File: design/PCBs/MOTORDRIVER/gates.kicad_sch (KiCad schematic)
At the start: 0 parts

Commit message: worked on motor pcb
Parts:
- added U4: 2ED1323S12P, Package_SO:Infineon_PG-DSO-20-U03_7.5x12.8mm, symbol Driver_FET:2ED1323S12P
- added U5: CPC1002N, Package_SO:SOP-4_3.8x4.1mm_P2.54mm, symbol Relay_SolidState:CPC1002N
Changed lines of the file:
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@@
 	(generator_version "8.0")
 	(paper "A4")
+	(symbol
+		(lib_id "Relay_SolidState:CPC1002N")
+		(at 153.67 73.66 0)
+		(unit 1)
+		(exclude_from_sim no)
+		(in_bom yes)
+		(on_board yes)
+		(dnp no)
+		(fields_autoplaced yes)
+		(property "Reference" "U5"
+			(at 153.67 64.77 0)
+			(effects
+				(font
+					(size 1.27 1.27)
+				)
+			)
+		)
+		(property "Value" "CPC1002N"
+			(at 153.67 67.31 0)
+			(effects
+				(font
+					(size 1.27 1.27)
+				)
+			)
+		)
+		(property "Footprint" "Package_SO:SOP-4_3.8x4.1mm_P2.54mm"
+			(at 148.59 78.74 0)
+			(effects
+				(font
+					(size 1.27 1.27)
+					(italic yes)
+				)
+				(justify left)
+				(hide yes)
+			)
+		)
+		(property "Datasheet" "http://www.ixysic.com/home/pdfs.nsf/www/CPC1002N.pdf/$file/CPC1002N.pdf"
+			(at 153.67 73.66 0)
+			(effects
+				(font
+					(size 1.27 1.27)
+				)
+				(justify left)
+				(hide yes)
+			)
+		)
+		(property "Description" "Form A, Solid State Relay (Photo MOSFET) 60V, 0.7A, 0.55Ohm, SOP-4"
+			(at 153.67 73.66 0)
+			(effects
+				(font
+					(size 1.27 1.27)
+				)
+				(hide yes)
+			)
+		)
+		(pin "2"
+		)
+		(pin "3"
+		)
+		(pin "1"
+		)
+		(pin "4"
+		)
+		(instances
+			(project ""
+				(path "/c7634e88-16d1-45ec-9aac-9c841e03cf6d/b5eb0271-9027-4941-b236-8f001fce8a08"
+					(reference "U5")
+					(unit 1)
+				)
+			)
+		)
+	)
+	(symbol
+		(lib_id "Driver_FET:2ED1323S12P")
+		(at 96.52 63.5 0)
+		(unit 1)
+		(exclude_from_sim no)
+		(in_bom yes)
+		(on_board yes)
+		(dnp no)
+		(fields_autoplaced yes)
+		(property "Reference" "U4"
+			(at 99.022 48.26 0)
+			(effects
+				(font
+					(size 1.27 1.27)
+				)
+				(justify left)
+			)
+		)
+		(property "Value" "2ED1323S12P"
+			(at 99.022 50.8 0)
+			(effects
+				(font
+					(size 1.27 1.27)
+				)
+				(justify left)
+			)
+		)
+		(property "Footprint" "Package_SO:Infineon_PG-DSO-20-U03_7.5x12.8mm"
+			(at 96.52 81.28 0)
+			(effects
+				(font
+					(size 1.27 1.27)
+					(italic yes)
+				)
+				(hide yes)
+			)
+		)
+		(property "Datasheet" "https://www.infineon.com/dgdl/Infineon-2ED1323S12P_2ED1324S12P-DataSheet-v01_01-EN.pdf?fileId=8ac78c8c869190210186e92f0f506d0c"
+			(at 97.79 78.74 0)
+			(effects
+				(font
+					(size 1.27 1.27)
+				)
+				(hide yes)
+			)
+		)
+		(property "Description" "1200V Half Bridge Gate Driver with active Miller clamp, OCP, SCC, Bootstrap Diode, +/-2.3A drive current, PG-DSO-20-U03"
+			(at 96.52 63.5 0)
+			(effects
+				(font
+					(size 1.27 1.27)
+				)
+				(hide yes)
+			)
+		)
+		(pin "9"
+		)
+		(pin "17"
+		)
+		(pin "4"
+		)
+		(pin "20"
+		)
+		(pin "3"
+		)
+		(pin "18"
+		)
+		(pin "7"
+		)
+		(pin "5"
+		)
+		(pin "6"
+		)
+		(pin "8"
+		)
+		(pin "16"
+		)
+		(pin "13"
+		)
+		(pin "2"
+		)
+		(pin "19"
+		)
+		(pin "10"
+		)
+		(pin "15"
+		)
+		(pin "14"
+		)
+		(pin "11"
+		)
+		(pin "1"
+		)
+		(pin "12"
+		)
+		(instances
+			(project ""
+				(path "/c7634e88-16d1-45ec-9aac-9c841e03cf6d/b5eb0271-9027-4941-b236-8f001fce8a08"
+					(reference "U4")
+					(unit 1)
+				)
+			)
+		)
+	)
 )

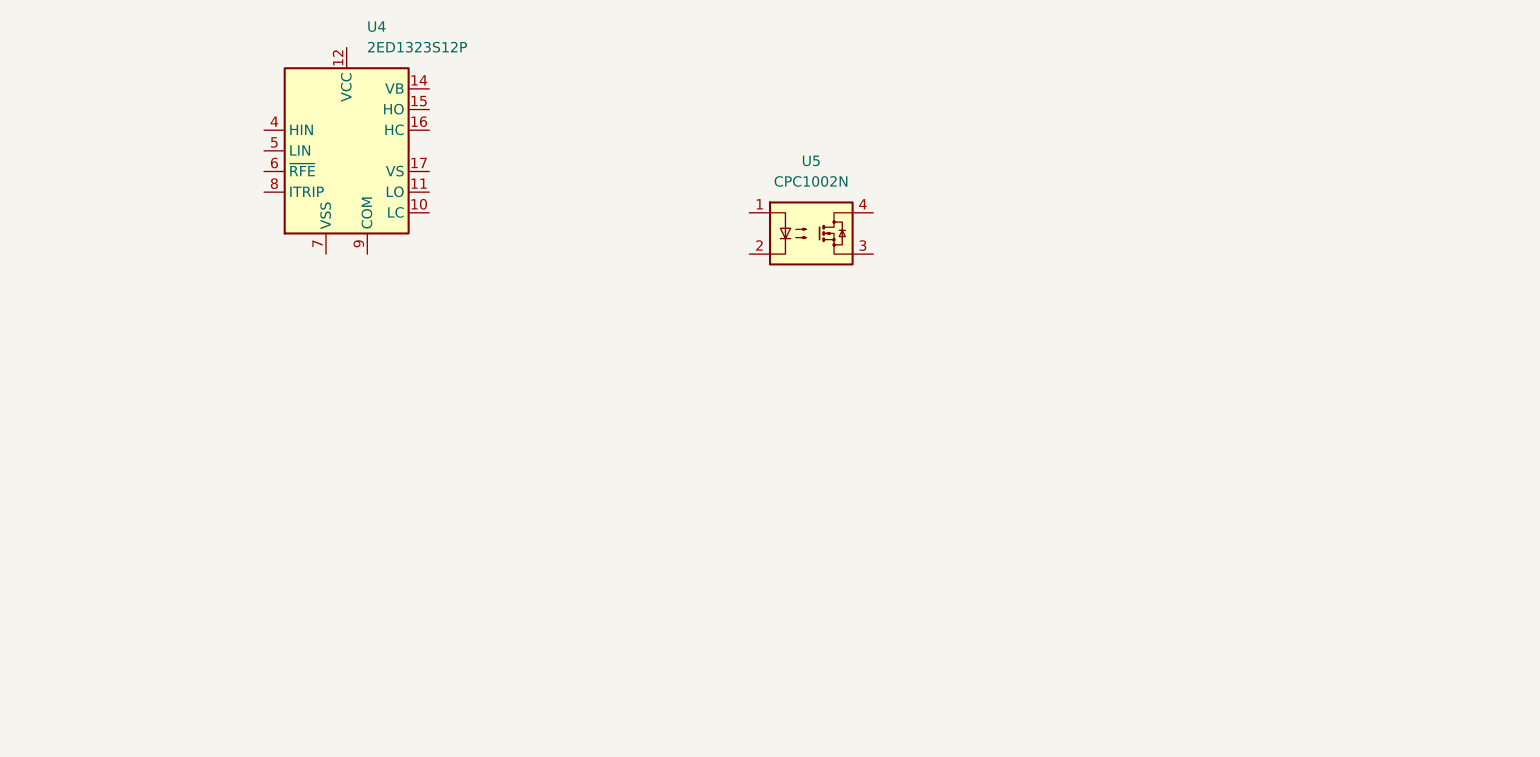
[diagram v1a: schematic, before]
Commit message: moved controller pcb to a single unified pcb, added more work on motordriver
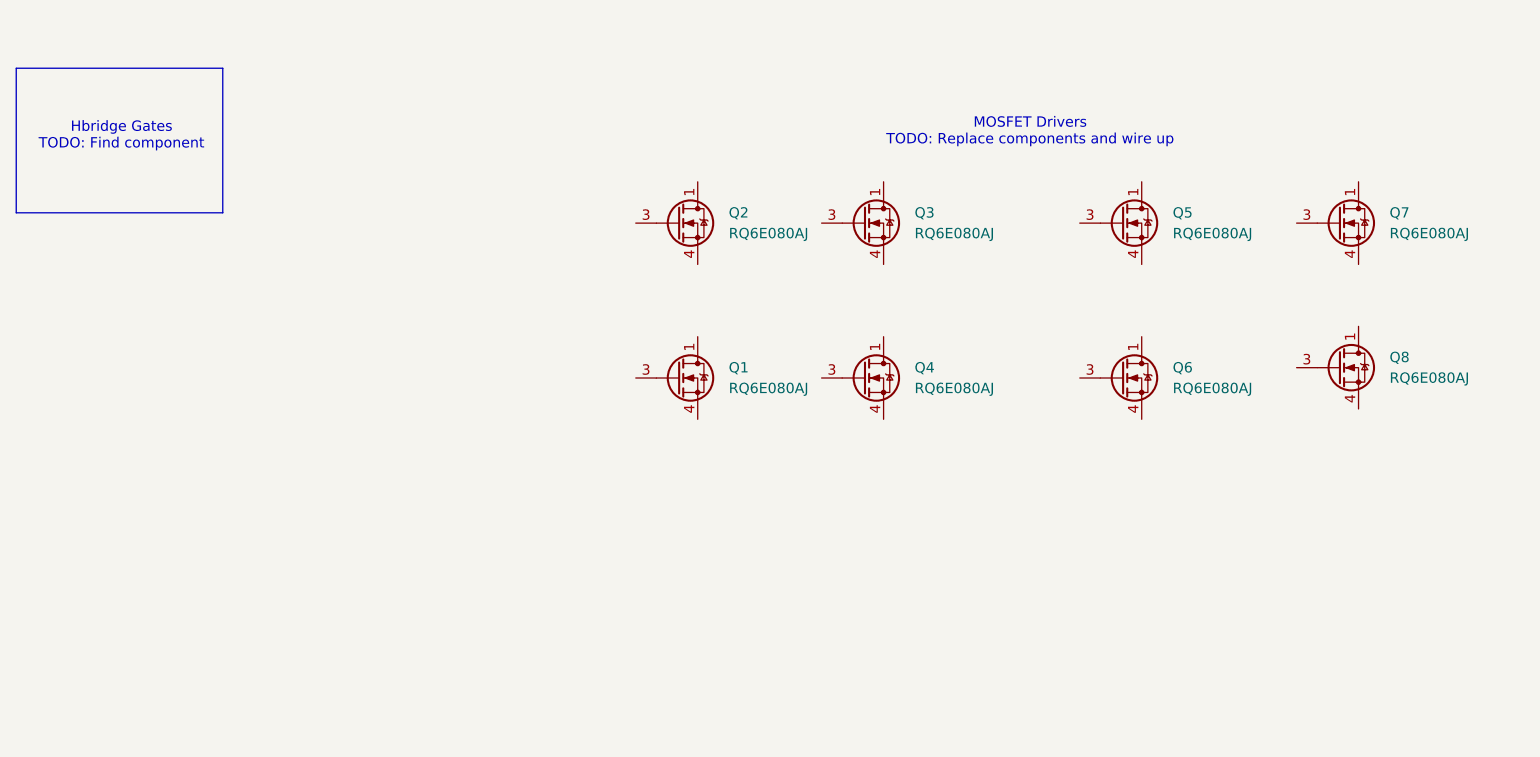
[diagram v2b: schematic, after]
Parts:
- removed U4: 2ED1323S12P, Package_SO:Infineon_PG-DSO-20-U03_7.5x12.8mm, symbol Driver_FET:2ED1323S12P
- removed U5: CPC1002N, Package_SO:SOP-4_3.8x4.1mm_P2.54mm, symbol Relay_SolidState:CPC1002N
- added Q1, Q2, Q3, Q4, Q5, Q6, Q7, Q8: RQ6E080AJ, Package_TO_SOT_SMD:TSOT-23-6, symbol Transistor_FET:RQ6E080AJ
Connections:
- new net: Q6.1 (D), Q6.2 (D), Q6.5 (D), Q6.6 (D)
- new net: Q4.1 (D), Q4.2 (D), Q4.5 (D), Q4.6 (D)
- new net: Q5.1 (D), Q5.2 (D), Q5.5 (D), Q5.6 (D)
- new net: Q7.1 (D), Q7.2 (D), Q7.5 (D), Q7.6 (D)
- new net: Q2.1 (D), Q2.2 (D), Q2.5 (D), Q2.6 (D)
- new net: Q8.1 (D), Q8.2 (D), Q8.5 (D), Q8.6 (D)
- new net: Q3.1 (D), Q3.2 (D), Q3.5 (D), Q3.6 (D)
- new net: Q1.1 (D), Q1.2 (D), Q1.5 (D), Q1.6 (D)
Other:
- note added: "Hbridge Gates TODO: Find component"
- note added: "MOSFET Drivers TODO: Replace components and wire up"

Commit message: updated PCB
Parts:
- renumbered Q1 to Q10
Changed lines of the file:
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@@
 		(instances
 			(project "motordriver"
+				(path "/c7634e88-16d1-45ec-9aac-9c841e03cf6d/4adc8e75-6797-461c-8ad6-e6b779b2e551"
+					(reference "Q22")
+					(unit 1)
+				)
 				(path "/c7634e88-16d1-45ec-9aac-9c841e03cf6d/b5eb0271-9027-4941-b236-8f001fce8a08"
 					(reference "Q6")
+					(unit 1)
+				)
+				(path "/c7634e88-16d1-45ec-9aac-9c841e03cf6d/d2c99155-6dc4-4cef-b7d8-f7ba5e4118d0"
+					(reference "Q14")
 					(unit 1)
 				)
@@
 		(instances
 			(project "motordriver"
+				(path "/c7634e88-16d1-45ec-9aac-9c841e03cf6d/4adc8e75-6797-461c-8ad6-e6b779b2e551"
+					(reference "Q20")
+					(unit 1)
+				)
 				(path "/c7634e88-16d1-45ec-9aac-9c841e03cf6d/b5eb0271-9027-4941-b236-8f001fce8a08"
 					(reference "Q4")
+					(unit 1)
+				)
+				(path "/c7634e88-16d1-45ec-9aac-9c841e03cf6d/d2c99155-6dc4-4cef-b7d8-f7ba5e4118d0"
+					(reference "Q12")
 					(unit 1)
 				)
@@
 		(instances
 			(project "motordriver"
+				(path "/c7634e88-16d1-45ec-9aac-9c841e03cf6d/4adc8e75-6797-461c-8ad6-e6b779b2e551"
+					(reference "Q21")
+					(unit 1)
+				)
 				(path "/c7634e88-16d1-45ec-9aac-9c841e03cf6d/b5eb0271-9027-4941-b236-8f001fce8a08"
 					(reference "Q5")
+					(unit 1)
+				)
+				(path "/c7634e88-16d1-45ec-9aac-9c841e03cf6d/d2c99155-6dc4-4cef-b7d8-f7ba5e4118d0"
+					(reference "Q13")
 					(unit 1)
 				)
@@
 		(instances
 			(project "motordriver"
+				(path "/c7634e88-16d1-45ec-9aac-9c841e03cf6d/4adc8e75-6797-461c-8ad6-e6b779b2e551"
+					(reference "Q23")
+					(unit 1)
+				)
 				(path "/c7634e88-16d1-45ec-9aac-9c841e03cf6d/b5eb0271-9027-4941-b236-8f001fce8a08"
 					(reference "Q7")
+					(unit 1)
+				)
+				(path "/c7634e88-16d1-45ec-9aac-9c841e03cf6d/d2c99155-6dc4-4cef-b7d8-f7ba5e4118d0"
+					(reference "Q15")
 					(unit 1)
 				)
@@
 		(instances
 			(project "motordriver"
+				(path "/c7634e88-16d1-45ec-9aac-9c841e03cf6d/4adc8e75-6797-461c-8ad6-e6b779b2e551"
+					(reference "Q17")
+					(unit 1)
+				)
 				(path "/c7634e88-16d1-45ec-9aac-9c841e03cf6d/b5eb0271-9027-4941-b236-8f001fce8a08"
 					(reference "Q2")
+					(unit 1)
+				)
+				(path "/c7634e88-16d1-45ec-9aac-9c841e03cf6d/d2c99155-6dc4-4cef-b7d8-f7ba5e4118d0"
+					(reference "Q9")
 					(unit 1)
 				)
@@
 		(instances
 			(project "motordriver"
+				(path "/c7634e88-16d1-45ec-9aac-9c841e03cf6d/4adc8e75-6797-461c-8ad6-e6b779b2e551"
+					(reference "Q24")
+					(unit 1)
+				)
 				(path "/c7634e88-16d1-45ec-9aac-9c841e03cf6d/b5eb0271-9027-4941-b236-8f001fce8a08"
 					(reference "Q8")
+					(unit 1)
+				)
+				(path "/c7634e88-16d1-45ec-9aac-9c841e03cf6d/d2c99155-6dc4-4cef-b7d8-f7ba5e4118d0"
+					(reference "Q16")
 					(unit 1)
 				)
@@
 		(instances
 			(project "motordriver"
+				(path "/c7634e88-16d1-45ec-9aac-9c841e03cf6d/4adc8e75-6797-461c-8ad6-e6b779b2e551"
+					(reference "Q19")
+					(unit 1)
+				)
 				(path "/c7634e88-16d1-45ec-9aac-9c841e03cf6d/b5eb0271-9027-4941-b236-8f001fce8a08"
 					(reference "Q3")
+					(unit 1)
+				)
+				(path "/c7634e88-16d1-45ec-9aac-9c841e03cf6d/d2c99155-6dc4-4cef-b7d8-f7ba5e4118d0"
+					(reference "Q11")
 					(unit 1)
 				)
@@
 		(dnp no)
 		(fields_autoplaced yes)
-		(property "Reference" "Q1"
+		(property "Reference" "Q10"
 			(at 143.51 90.1699 0)
 			(effects
@@
 		)
 		(instances
-			(project ""
-				(path "/c7634e88-16d1-45ec-9aac-9c841e03cf6d/b5eb0271-9027-4941-b236-8f001fce8a08"
-					(reference "Q1")
-					(unit 1)
-				)
+			(project "motordriver"
+				(path "/c7634e88-16d1-45ec-9aac-9c841e03cf6d/4adc8e75-6797-461c-8ad6-e6b779b2e551"
+					(reference "Q18")
+					(unit 1)
+				)
+				(path "/c7634e88-16d1-45ec-9aac-9c841e03cf6d/d2c99155-6dc4-4cef-b7d8-f7ba5e4118d0"
+					(reference "Q10")
+					(unit 1)
+				)

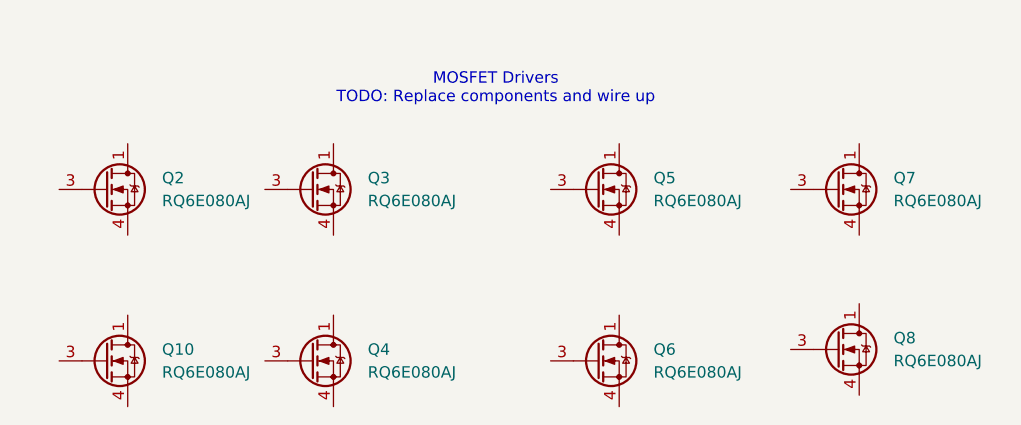
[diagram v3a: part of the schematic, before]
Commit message: added programmer
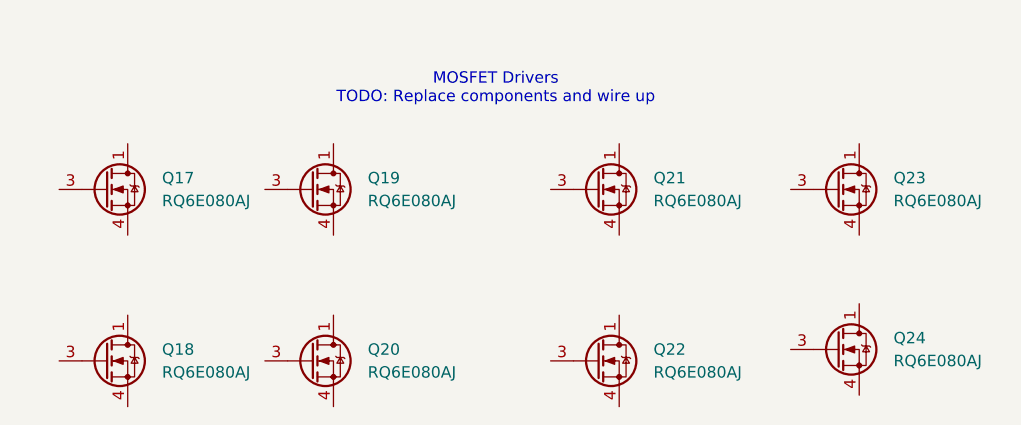
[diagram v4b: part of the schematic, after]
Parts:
- renumbered Q2 to Q17, Q10 to Q18, Q3 to Q19, Q4 to Q20, Q5 to Q21, Q6 to Q22, Q7 to Q23, Q8 to Q24
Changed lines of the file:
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@@
 		(dnp no)
 		(fields_autoplaced yes)
-		(property "Reference" "Q6"
+		(property "Reference" "Q22"
 			(at 198.12 90.1699 0)
 			(effects
@@
 		(dnp no)
 		(fields_autoplaced yes)
-		(property "Reference" "Q4"
+		(property "Reference" "Q20"
 			(at 166.37 90.1699 0)
 			(effects
@@
 		(dnp no)
 		(fields_autoplaced yes)
-		(property "Reference" "Q5"
+		(property "Reference" "Q21"
 			(at 198.12 71.1199 0)
 			(effects
@@
 		(dnp no)
 		(fields_autoplaced yes)
-		(property "Reference" "Q7"
+		(property "Reference" "Q23"
 			(at 224.79 71.1199 0)
 			(effects
@@
 		(dnp no)
 		(fields_autoplaced yes)
-		(property "Reference" "Q2"
+		(property "Reference" "Q17"
 			(at 143.51 71.1199 0)
 			(effects
@@
 		(dnp no)
 		(fields_autoplaced yes)
-		(property "Reference" "Q8"
+		(property "Reference" "Q24"
 			(at 224.79 88.8999 0)
 			(effects
@@
 		(dnp no)
 		(fields_autoplaced yes)
-		(property "Reference" "Q3"
+		(property "Reference" "Q19"
 			(at 166.37 71.1199 0)
 			(effects
@@
 		(dnp no)
 		(fields_autoplaced yes)
-		(property "Reference" "Q10"
+		(property "Reference" "Q18"
 			(at 143.51 90.1699 0)
 			(effects
@@
 					(unit 1)
 				)
+				(path "/c7634e88-16d1-45ec-9aac-9c841e03cf6d/b5eb0271-9027-4941-b236-8f001fce8a08"
+					(reference "Q?")
+					(unit 1)
+				)

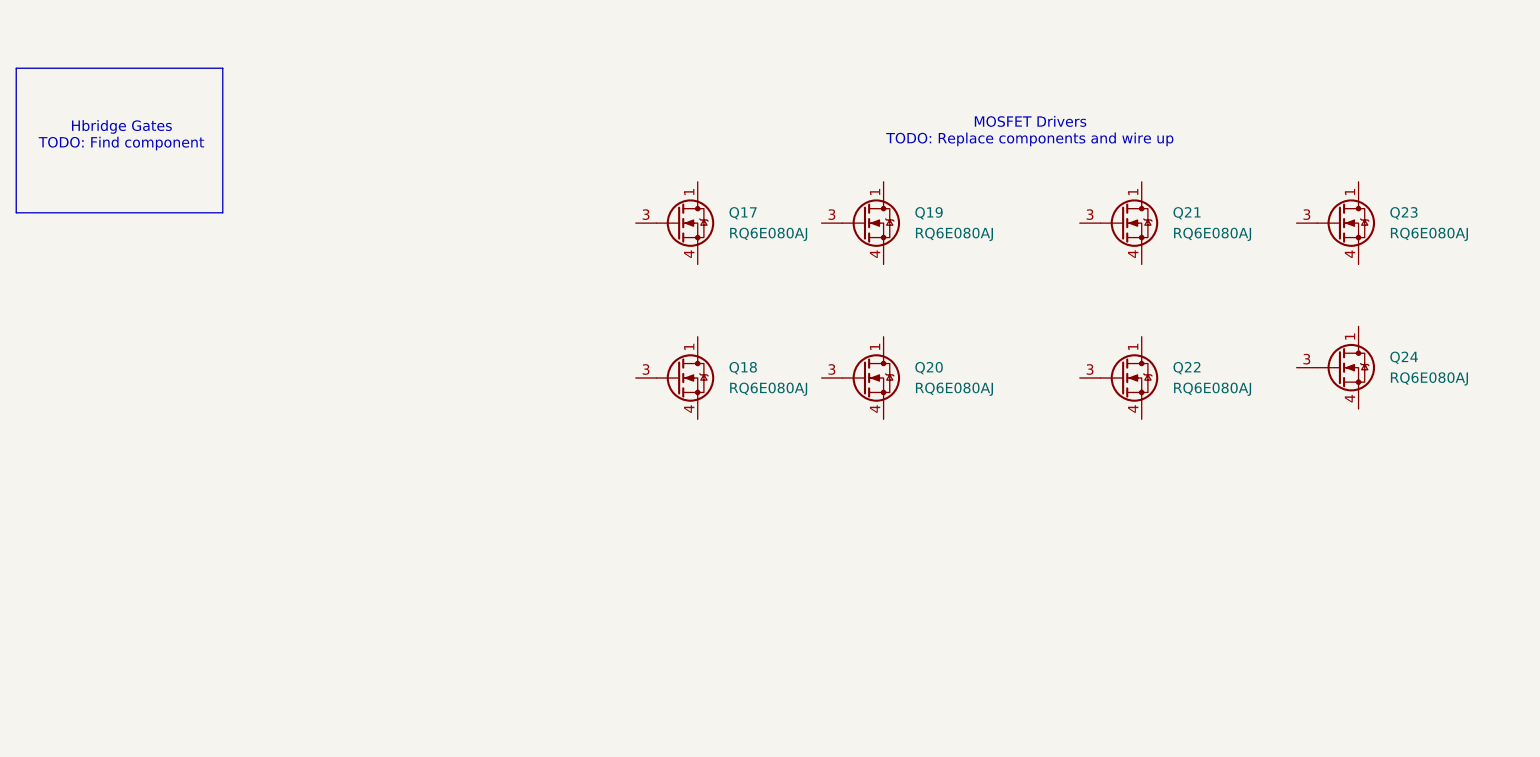
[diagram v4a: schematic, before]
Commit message: Clearer file names for datasheets indicating what kind of component they are. Started on connecting the battery charger Added mosfet ICs for driver gates
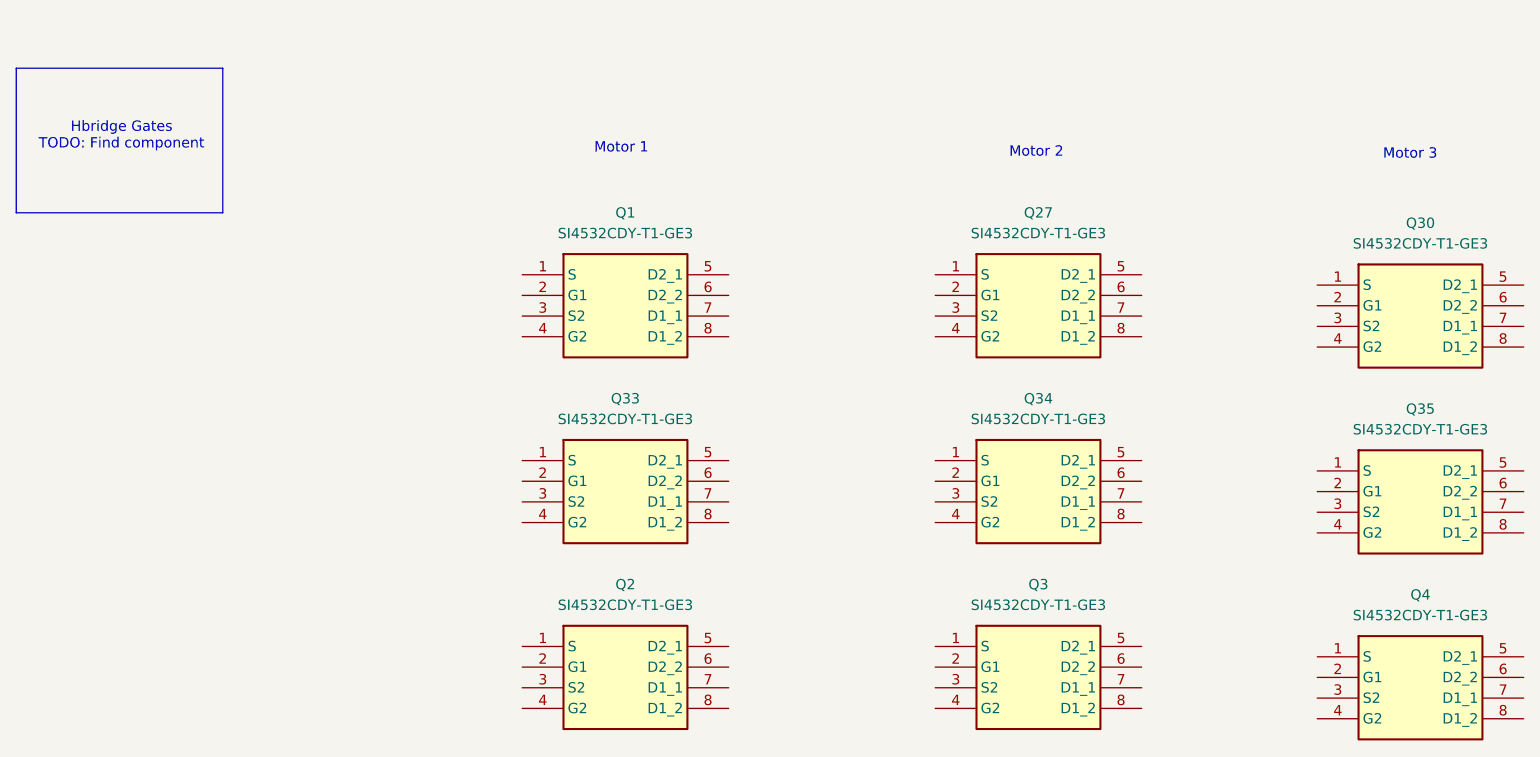
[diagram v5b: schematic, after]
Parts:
- removed Q17, Q18, Q19, Q20, Q21, Q22, Q23, Q24: RQ6E080AJ, Package_TO_SOT_SMD:TSOT-23-6, symbol Transistor_FET:RQ6E080AJ
- added Q1, Q2, Q27, Q3, Q30, Q33, Q34, Q35, Q4: SI4532CDY-T1-GE3, SOT127P600X175-8N, symbol SI4532CDY-T1-GE3:SI4532CDY-T1-GE3
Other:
- note added: "Motor 1"
- note added: "Motor 2"
- note added: "Motor 3"
- note removed: "MOSFET Drivers TODO: Replace components and wire up"
